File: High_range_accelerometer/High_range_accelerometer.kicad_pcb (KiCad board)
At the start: 2 copper layers, 30 x 70 mm, 59 parts, among them J1 USB_B_Micro, J2 Micro_SD_Card_Det_Hirose_DM3AT, P1 KRC_PSoCWriter, U1 KRC_Conn_CAN, U2 NCP718ASN330T1G, U3 NCP718ASN500T1G, U4 NCV7342, U5 CY8C5868LTI-LP039, U6 H3LIS331DLTR, U7 W25N01GVxxIG-IT, Y2 Crystal_MHz

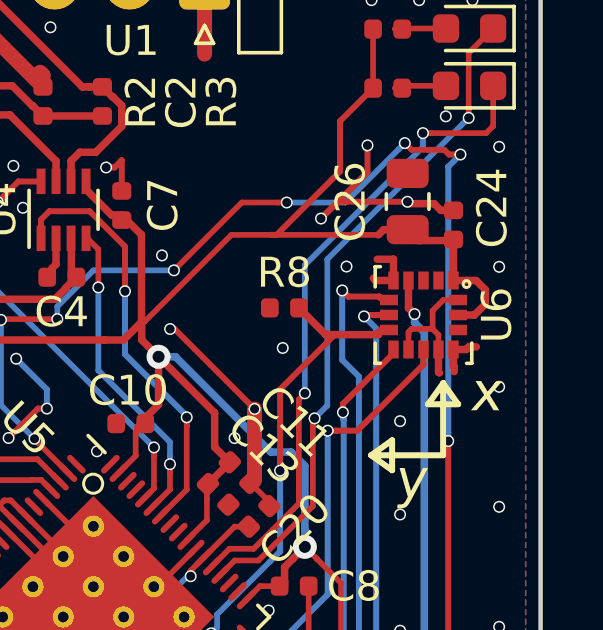
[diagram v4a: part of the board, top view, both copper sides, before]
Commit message: modified sensor footprint
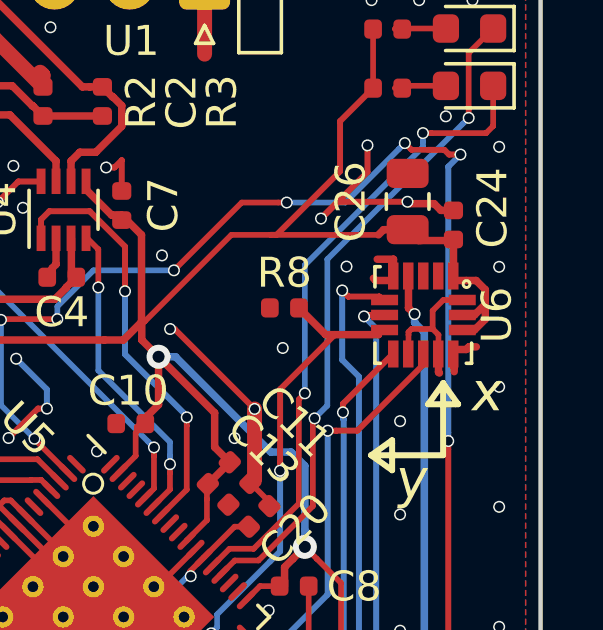
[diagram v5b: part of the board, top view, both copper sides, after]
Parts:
- U6: footprint Package_LGA:LGA-16_3x3mm_P0.5mm_LayoutBorder3x5y -> my_footprint:LGA-16_3x3mm_P0.5mm_LayoutBorder3x5y_handsoldering
- moved G*** 15.0 mm to (115.6, 67.2)
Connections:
- U6 pad 14: (no net) -> +3V3
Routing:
- net +3V3: track 149.6 -> 151.2 mm
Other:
- board text added: "rev. 1.3"
- board text removed: "rev. 1.2"
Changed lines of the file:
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@@
     (thickness 1.6)
     (drawings 52)
-    (tracks 874)
+    (tracks 877)
     (zones 0)
     (modules 59)
@@
     (34 B.Paste user)
     (35 F.Paste user)
-    (36 B.SilkS user hide)
+    (36 B.SilkS user)
     (37 F.SilkS user)
     (38 B.Mask user)
@@
       (padsonsilk false)
       (subtractmaskfromsilk false)
-      (outputformat 5)
+      (outputformat 1)
       (mirror false)
       (drillshape 0)
       (scaleselection 1)
-      (outputdirectory "SVG/"))
+      (outputdirectory "Gearber/"))
   )
   (net 0 "")
@@
     )
   )
-  (module Package_LGA:LGA-16_3x3mm_P0.5mm_LayoutBorder3x5y (layer F.Cu)
-    (at 117.9449 73.62444 270)
-    (descr "LGA, 16 Pin (http://www.st.com/resource/en/datasheet/lis331hh.pdf), generated with kicad-footprint-generator ipc_lga_layoutBorder_generator.py")
-    (tags "LGA LGA")
-    (attr smd)
-    (fp_text reference U6 (at 0 -2.45 90) (layer F.SilkS)
-      (effects (font (size 1 1) (thickness 0.15)))
-    )
-    (fp_text value H3LIS331DLTR (at 0 2.45 90) (layer F.Fab)
-      (effects (font (size 1 1) (thickness 0.15)))
-    )
-    (fp_line (start 0.935 -1.61) (end 1.61 -1.61) (layer F.SilkS) (width 0.12))
-    (fp_line (start 1.61 -1.61) (end 1.61 -1.435) (layer F.SilkS) (width 0.12))
-    (fp_line (start 0.935 1.61) (end 1.61 1.61) (layer F.SilkS) (width 0.12))
-    (fp_line (start 1.61 1.61) (end 1.61 1.435) (layer F.SilkS) (width 0.12))
-    (fp_line (start -0.935 1.61) (end -1.61 1.61) (layer F.SilkS) (width 0.12))
-    (fp_line (start -1.61 1.61) (end -1.61 1.435) (layer F.SilkS) (width 0.12))
-    (fp_line (start -0.75 -1.5) (end 1.5 -1.5) (layer F.Fab) (width 0.1))
-    (fp_line (start 1.5 -1.5) (end 1.5 1.5) (layer F.Fab) (width 0.1))
-    (fp_line (start 1.5 1.5) (end -1.5 1.5) (layer F.Fab) (width 0.1))
-    (fp_line (start -1.5 1.5) (end -1.5 -0.75) (layer F.Fab) (width 0.1))
-    (fp_line (start -1.5 -0.75) (end -0.75 -1.5) (layer F.Fab) (width 0.1))
-    (fp_line (start -1.75 -1.75) (end -1.75 1.75) (layer F.CrtYd) (width 0.05))
-    (fp_line (start -1.75 1.75) (end 1.75 1.75) (layer F.CrtYd) (width 0.05))
-    (fp_line (start 1.75 1.75) (end 1.75 -1.75) (layer F.CrtYd) (width 0.05))
-    (fp_line (start 1.75 -1.75) (end -1.75 -1.75) (layer F.CrtYd) (width 0.05))
-    (fp_text user %R (at 0 0 90) (layer F.Fab)
-      (effects (font (size 0.75 0.75) (thickness 0.11)))
-    )
-    (pad 1 smd rect (at -1.15 -1 270) (size 0.6 0.35) (layers F.Cu F.Paste F.Mask)
-      (net 5 +3V3))
-    (pad 2 smd rect (at -1.15 -0.5 270) (size 0.6 0.35) (layers F.Cu F.Paste F.Mask))
-    (pad 3 smd rect (at -1.15 0 270) (size 0.6 0.35) (layers F.Cu F.Paste F.Mask))
-    (pad 4 smd rect (at -1.15 0.5 270) (size 0.6 0.35) (layers F.Cu F.Paste F.Mask)
-      (net 32 Sensor-CLK))
-    (pad 5 smd rect (at -1.15 1 270) (size 0.6 0.35) (layers F.Cu F.Paste F.Mask)
-      (net 2 GND))
-    (pad 6 smd rect (at -0.5 1.15 270) (size 0.35 0.6) (layers F.Cu F.Paste F.Mask)
-      (net 33 Sensor-MOSI))
-    (pad 7 smd rect (at 0 1.15 270) (size 0.35 0.6) (layers F.Cu F.Paste F.Mask)
-      (net 34 Sensor-MISO))
-    (pad 8 smd rect (at 0.5 1.15 270) (size 0.35 0.6) (layers F.Cu F.Paste F.Mask)
-      (net 22 Sensor-CS))
-    (pad 9 smd rect (at 1.15 1 270) (size 0.6 0.35) (layers F.Cu F.Paste F.Mask)
-      (net 35 INT1))
-    (pad 10 smd rect (at 1.15 0.5 270) (size 0.6 0.35) (layers F.Cu F.Paste F.Mask)
-      (net 2 GND))
-    (pad 11 smd rect (at 1.15 0 270) (size 0.6 0.35) (layers F.Cu F.Paste F.Mask)
-      (net 36 INT2))
-    (pad 12 smd rect (at 1.15 -0.5 270) (size 0.6 0.35) (layers F.Cu F.Paste F.Mask)
-      (net 2 GND))
-    (pad 13 smd rect (at 1.15 -1 270) (size 0.6 0.35) (layers F.Cu F.Paste F.Mask)
-      (net 2 GND))
-    (pad 14 smd rect (at 0.5 -1.15 270) (size 0.35 0.6) (layers F.Cu F.Paste F.Mask))
-    (pad 15 smd rect (at 0 -1.15 270) (size 0.35 0.6) (layers F.Cu F.Paste F.Mask)
-      (net 5 +3V3))
-    (pad 16 smd rect (at -0.5 -1.15 270) (size 0.35 0.6) (layers F.Cu F.Paste F.Mask)
-      (net 2 GND))
-    (model ${KISYS3DMOD}/Package_LGA.3dshapes/LGA-16_3x3mm_P0.5mm_LayoutBorder3x5y.wrl
-      (at (xyz 0 0 0))
-      (scale (xyz 1 1 1))
-      (rotate (xyz 0 0 0))
-    )
-  )
   (module KUTKiCad_footprint:WSON-8_8x6mm_P1.27mm (layer F.Cu)
     (at 106.59872 107.57916)
@@
   )
   (module my_footprint:Twitter_logo (layer B.Cu)
-    (at 115.6462 82.2198 90)
+    (at 115.5954 67.2084 90)
     (fp_text reference G*** (at 0 0 90) (layer B.SilkS) hide
       (effects (font (size 1.524 1.524) (thickness 0.3)) (justify mirror))
@@
       (xy -6.229974 -2.276739) (xy -6.202883 -2.270457) (xy -6.167082 -2.268653) (xy -6.121371 -2.269066)) (layer B.SilkS) (width 0.01))
   )
+  (module my_footprint:LGA-16_3x3mm_P0.5mm_LayoutBorder3x5y_handsoldering (layer F.Cu)
+    (at 117.93728 73.62444 270)
+    (descr "LGA, 16 Pin (http://www.st.com/resource/en/datasheet/lis331hh.pdf), generated with kicad-footprint-generator ipc_lga_layoutBorder_generator.py")
+    (tags "LGA LGA")
+    (attr smd)
+    (fp_text reference U6 (at 0 -2.45 90) (layer F.SilkS)
+      (effects (font (size 1 1) (thickness 0.15)))
+    )
+    (fp_text value H3LIS331DLTR (at 0 2.45 90) (layer F.Fab)
+      (effects (font (size 1 1) (thickness 0.15)))
+    )
+    (fp_line (start 0.935 -1.61) (end 1.61 -1.61) (layer F.SilkS) (width 0.12))
+    (fp_line (start 1.61 -1.61) (end 1.61 -1.435) (layer F.SilkS) (width 0.12))
+    (fp_line (start 0.935 1.61) (end 1.61 1.61) (layer F.SilkS) (width 0.12))
+    (fp_line (start 1.61 1.61) (end 1.61 1.435) (layer F.SilkS) (width 0.12))
+    (fp_line (start -0.935 1.61) (end -1.61 1.61) (layer F.SilkS) (width 0.12))
+    (fp_line (start -1.61 1.61) (end -1.61 1.435) (layer F.SilkS) (width 0.12))
+    (fp_line (start -0.75 -1.5) (end 1.5 -1.5) (layer F.Fab) (width 0.1))
+    (fp_line (start 1.5 -1.5) (end 1.5 1.5) (layer F.Fab) (width 0.1))
+    (fp_line (start 1.5 1.5) (end -1.5 1.5) (layer F.Fab) (width 0.1))
+    (fp_line (start -1.5 1.5) (end -1.5 -0.75) (layer F.Fab) (width 0.1))
+    (fp_line (start -1.5 -0.75) (end -0.75 -1.5) (layer F.Fab) (width 0.1))
+    (fp_line (start -1.75 -1.75) (end -1.75 1.75) (layer F.CrtYd) (width 0.05))
+    (fp_line (start -1.75 1.75) (end 1.75 1.75) (layer F.CrtYd) (width 0.05))
+    (fp_line (start 1.75 1.75) (end 1.75 -1.75) (layer F.CrtYd) (width 0.05))
+    (fp_line (start 1.75 -1.75) (end -1.75 -1.75) (layer F.CrtYd) (width 0.05))
+    (fp_text user %R (at 0 0 90) (layer F.Fab)
+      (effects (font (size 0.75 0.75) (thickness 0.11)))
+    )
+    (pad 1 smd rect (at -1.3 -1 270) (size 0.9 0.35) (layers F.Cu F.Paste F.Mask)
+      (net 5 +3V3))
+    (pad 2 smd rect (at -1.3 -0.5 270) (size 0.9 0.35) (layers F.Cu F.Paste F.Mask))
+    (pad 3 smd rect (at -1.3 0 270) (size 0.9 0.35) (layers F.Cu F.Paste F.Mask))
+    (pad 4 smd rect (at -1.3 0.5 270) (size 0.9 0.35) (layers F.Cu F.Paste F.Mask)
+      (net 32 Sensor-CLK))
+    (pad 5 smd rect (at -1.3 1 270) (size 0.9 0.35) (layers F.Cu F.Paste F.Mask)
+      (net 2 GND))
+    (pad 6 smd rect (at -0.5 1.29 270) (size 0.35 0.9) (layers F.Cu F.Paste F.Mask)
+      (net 33 Sensor-MOSI))
+    (pad 7 smd rect (at 0 1.29 270) (size 0.35 0.9) (layers F.Cu F.Paste F.Mask)
+      (net 34 Sensor-MISO))
+    (pad 8 smd rect (at 0.5 1.29 270) (size 0.35 0.9) (layers F.Cu F.Paste F.Mask)
+      (net 22 Sensor-CS))
+    (pad 9 smd rect (at 1.3 1 270) (size 0.9 0.35) (layers F.Cu F.Paste F.Mask)
+      (net 35 INT1))
+    (pad 10 smd rect (at 1.3 0.5 270) (size 0.9 0.35) (layers F.Cu F.Paste F.Mask)
+      (net 2 GND))
+    (pad 11 smd rect (at 1.3 0 270) (size 0.9 0.35) (layers F.Cu F.Paste F.Mask)
+      (net 36 INT2))
+    (pad 12 smd rect (at 1.3 -0.5 270) (size 0.9 0.35) (layers F.Cu F.Paste F.Mask)
+      (net 2 GND))
+    (pad 13 smd rect (at 1.3 -1 270) (size 0.9 0.35) (layers F.Cu F.Paste F.Mask)
+      (net 2 GND))
+    (pad 14 smd rect (at 0.5 -1.3 270) (size 0.35 0.9) (layers F.Cu F.Paste F.Mask)
+      (net 5 +3V3))
+    (pad 15 smd rect (at 0 -1.3 270) (size 0.35 0.9) (layers F.Cu F.Paste F.Mask)
+      (net 5 +3V3))
+    (pad 16 smd rect (at -0.5 -1.3 270) (size 0.35 0.9) (layers F.Cu F.Paste F.Mask)
+      (net 2 GND))
+    (model ${KISYS3DMOD}/Package_LGA.3dshapes/LGA-16_3x3mm_P0.5mm_LayoutBorder3x5y.wrl
+      (at (xyz 0 0 0))
+      (scale (xyz 1 1 1))
+      (rotate (xyz 0 0 0))
+    )
+  )
   (gr_circle (center 106.934 79.248) (end 107.252261 79.248) (layer F.SilkS) (width 0.1))
-  (gr_text "rev. 1.2" (at 119.9896 61.595 270) (layer B.SilkS)
+  (gr_text "rev. 1.3" (at 119.9642 61.595 270) (layer B.SilkS)
     (effects (font (size 1 1) (thickness 0.15)) (justify mirror))
   )
@@
     (effects (font (size 1 1) (thickness 0.15)) (justify mirror))
   )
-  (gr_text @Malus_Mill_ (at 112.5266 82.2388 270) (layer B.SilkS)
+  (gr_text @Malus_Mill_ (at 113.0808 67.4878 270) (layer B.SilkS)
     (effects (font (size 1 1) (thickness 0.15)) (justify mirror))
   )
   (gr_circle (center 103.8 105.15) (end 103.55 105.35) (layer F.SilkS) (width 0.2))
-  (gr_text "Designed by ringo" (at 120 89.45 270) (layer B.SilkS)
+  (gr_text "Designed by ringo" (at 119.9642 80.2894 270) (layer B.SilkS)
     (effects (font (size 1 1) (thickness 0.15)) (justify left mirror))
   )
@@
   (segment (start 116.26492 66.06286) (end 115.1636 67.16418) (width 0.2) (layer F.Cu) (net 5))
   (segment (start 115.1636 67.16418) (end 115.1636 68.837402) (width 0.2) (layer F.Cu) (net 5))
+  (segment (start 120.00558 73.76376) (end 120.00558 73.26376) (width 0.25) (layer F.Cu) (net 5))
+  (segment (start 119.6449 74.12444) (end 120.00558 73.76376) (width 0.25) (layer F.Cu) (net 5))
+  (segment (start 119.0949 74.12444) (end 119.6449 74.12444) (width 0.25) (layer F.Cu) (net 5))
   (segment (start 109.98962 87.303306) (end 109.98962 89.16416) (width 0.19) (layer F.Cu) (net 6) (status 20))
   (segment (start 109.487384 86.80107) (end 109.98962 87.303306) (width 0.19) (layer F.Cu) (net 6) (status 10))
